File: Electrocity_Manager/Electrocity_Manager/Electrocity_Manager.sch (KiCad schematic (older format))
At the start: 187 parts, among them IC2 MAIN_SHUTDOWN, IC3 RELAY_STATE, IC4 ADC_RST, J1 SERIAL, P1 SWD, P10 EMERGENCY, P11 EMERGENCY, P12 FRAME_GRAND, P13 BATT_IN, P14 POWER_OUT, P15 FUN_OUT, P16 BATT_IN, P17 POWER_OUT, P18 FUN_OUT, P2 CAN, P3 CAN, P4 EMERGENCY_SIGNAL, P5 EMERGENCY_SIGNAL, P6 12V_OUT, P7 12V_OUT, P9 MAIN_SW, Q1 FET_N, Q2 NPN, Q3 NPN, Q7 FET_N, SW1 RST, SW2 SW0, SW3 SW1, U1 MAX3051, U10 BD9G101G, U11 ACS781, U12 V23134J1052D642, U13 ACS70331, U14 ACS781, U15 BD33FA1, U16 LOGO, U17 LOGO, U18 LOGO, U19 MCP2221A, U2 STM32F405RG, U20 OSRB38C9AA, U21 OSRB38C9AA, U22 HSIN_946, U23 LOGO, U3 FULL COLOR, U4 AQM0802_BL, U5 AP3211, U6 SI8900, U7 AZ1086H, U8 V23134J1052D642, U9 RPA60-12FW/P, X1 8MHz

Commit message: 緑ピカチュウか何か
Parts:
- added U24: LOGO, Mizz_lib:Pikatyuu_15x15, symbol Electrocity_Manager-rescue:LOGO-myDevice
- added U25: LOGO, Mizz_lib:MonsterBall_10x10_silk, symbol Electrocity_Manager-rescue:LOGO-myDevice
- added U26: LOGO, Mizz_lib:PiOtyu_silk_21.3x6.8, symbol Electrocity_Manager-rescue:LOGO-myDevice
- C32: value 470u -> 220u
- C35: value 470u -> 100u
- U9: value RPA60-12FW/P -> RPA60-12FW/N
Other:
- moved on the sheet: U16, U17, U18, U23
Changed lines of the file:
@@
 P 12675 8025
 F 0 "U9" H 12675 8590 50  0000 C CNN
-F 1 "RPA60-12FW/P" H 12675 8499 50  0000 C CNN
+F 1 "RPA60-12FW/N" H 12675 8499 50  0000 C CNN
 F 2 "Mizz_lib:RPA60-24xxSFW" H 12675 8025 50  0001 C CNN
 F 3 "" H 12675 8025 50  0001 C CNN
@@
 P 11825 7975
 F 0 "C32" H 11850 8075 50  0000 L CNN
-F 1 "470u" H 11850 7875 50  0000 L CNN
+F 1 "220u" H 11850 7875 50  0000 L CNN
 F 2 "Capacitors_ThroughHole:C_Radial_D6.3_L11.2_P2.5" H 11825 7975 60  0001 C CNN
 F 3 "" H 11825 7975 60  0000 C CNN
@@
 P 13525 7925
 F 0 "C35" H 13425 7825 50  0000 L CNN
-F 1 "470u" H 13325 8100 50  0000 L CNN
+F 1 "100u" H 13325 8100 50  0000 L CNN
 F 2 "Capacitors_ThroughHole:C_Radial_D6.3_L11.2_P2.5" H 13525 7925 60  0001 C CNN
 F 3 "" H 13525 7925 60  0000 C CNN
@@
 L Electrocity_Manager-rescue:LOGO-myDevice U17
 U 1 1 5D1B0D5D
-P 15475 800
-F 0 "U17" H 15753 853 60  0000 L CNN
-F 1 "LOGO" H 15753 747 60  0000 L CNN
-F 2 "Mizz_lib:Power_logo_Silk_5x5" H 15475 800 60  0001 C CNN
-F 3 "" H 15475 800 60  0000 C CNN
-	1    15475 800
+P 15525 800
+F 0 "U17" H 15803 853 60  0000 L CNN
+F 1 "LOGO" H 15803 747 60  0000 L CNN
+F 2 "Mizz_lib:Power_logo_Silk_5x5" H 15525 800 60  0001 C CNN
+F 3 "" H 15525 800 60  0000 C CNN
+	1    15525 800
 	1    0    0    -1
 $EndComp
@@
 L Electrocity_Manager-rescue:LOGO-myDevice U18
 U 1 1 5D1B1113
-P 15475 1375
-F 0 "U18" H 15753 1428 60  0000 L CNN
-F 1 "LOGO" H 15753 1322 60  0000 L CNN
-F 2 "Mizz_lib:Mini_Monster" H 15475 1375 60  0001 C CNN
-F 3 "" H 15475 1375 60  0000 C CNN
-	1    15475 1375
+P 15525 1375
+F 0 "U18" H 15803 1428 60  0000 L CNN
+F 1 "LOGO" H 15803 1322 60  0000 L CNN
+F 2 "Mizz_lib:Mini_Monster" H 15525 1375 60  0001 C CNN
+F 3 "" H 15525 1375 60  0000 C CNN
+	1    15525 1375
 	1    0    0    -1
 $EndComp
@@
 L Electrocity_Manager-rescue:LOGO-myDevice U16
 U 1 1 5CD3E880
-P 15475 1950
-F 0 "U16" H 15753 2003 60  0000 L CNN
-F 1 "LOGO" H 15753 1897 60  0000 L CNN
-F 2 "Mizz_lib:Robocon2019_30.0x30.0_silk" H 15475 1950 60  0001 C CNN
-F 3 "" H 15475 1950 60  0000 C CNN
-	1    15475 1950
+P 15525 1950
+F 0 "U16" H 15803 2003 60  0000 L CNN
+F 1 "LOGO" H 15803 1897 60  0000 L CNN
+F 2 "Mizz_lib:Robocon2019_30.0x30.0_silk" H 15525 1950 60  0001 C CNN
+F 3 "" H 15525 1950 60  0000 C CNN
+	1    15525 1950
 	1    0    0    -1
 $EndComp
@@
 L Electrocity_Manager-rescue:LOGO-myDevice U23
 U 1 1 5CD3FB17
-P 15475 2525
-F 0 "U23" H 15753 2578 60  0000 L CNN
-F 1 "LOGO" H 15753 2472 60  0000 L CNN
-F 2 "Mizz_lib:Battery_Killer_logo" H 15475 2525 60  0001 C CNN
-F 3 "" H 15475 2525 60  0000 C CNN
-	1    15475 2525
+P 15525 2525
+F 0 "U23" H 15803 2578 60  0000 L CNN
+F 1 "LOGO" H 15803 2472 60  0000 L CNN
+F 2 "Mizz_lib:Battery_Killer_logo" H 15525 2525 60  0001 C CNN
+F 3 "" H 15525 2525 60  0000 C CNN
+	1    15525 2525
 	1    0    0    -1
 $EndComp
@@
 	11800 6650 12000 6650
 Connection ~ 12000 6650
+$Comp
+L Electrocity_Manager-rescue:LOGO-myDevice U24
+U 1 1 5CC98F30
+P 15525 3100
+F 0 "U24" H 15803 3153 60  0000 L CNN
+F 1 "LOGO" H 15803 3047 60  0000 L CNN
+F 2 "Mizz_lib:Pikatyuu_15x15" H 15525 3100 60  0001 C CNN
+F 3 "" H 15525 3100 60  0000 C CNN
+	1    15525 3100
+	1    0    0    -1
+$EndComp
+$Comp
+L Electrocity_Manager-rescue:LOGO-myDevice U25
+U 1 1 5CC9B168
+P 15525 3700
+F 0 "U25" H 15803 3753 60  0000 L CNN
+F 1 "LOGO" H 15803 3647 60  0000 L CNN
+F 2 "Mizz_lib:MonsterBall_10x10_silk" H 15525 3700 60  0001 C CNN
+F 3 "" H 15525 3700 60  0000 C CNN
+	1    15525 3700
+	1    0    0    -1
+$EndComp
+$Comp
+L Electrocity_Manager-rescue:LOGO-myDevice U26
+U 1 1 5CC9CF8E
+P 15525 4300
+F 0 "U26" H 15803 4353 60  0000 L CNN
+F 1 "LOGO" H 15803 4247 60  0000 L CNN
+F 2 "Mizz_lib:PiOtyu_silk_21.3x6.8" H 15525 4300 60  0001 C CNN
+F 3 "" H 15525 4300 60  0000 C CNN
+	1    15525 4300
+	1    0    0    -1
+$EndComp
 $EndSCHEMATC

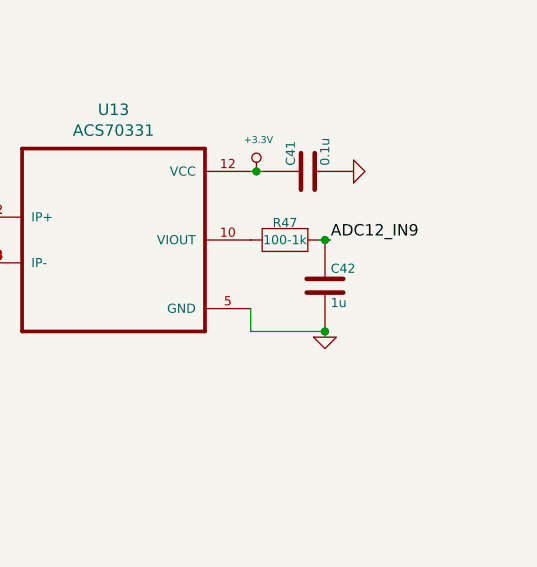
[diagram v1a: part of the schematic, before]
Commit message: ピカチュウたちの配線を変えた。
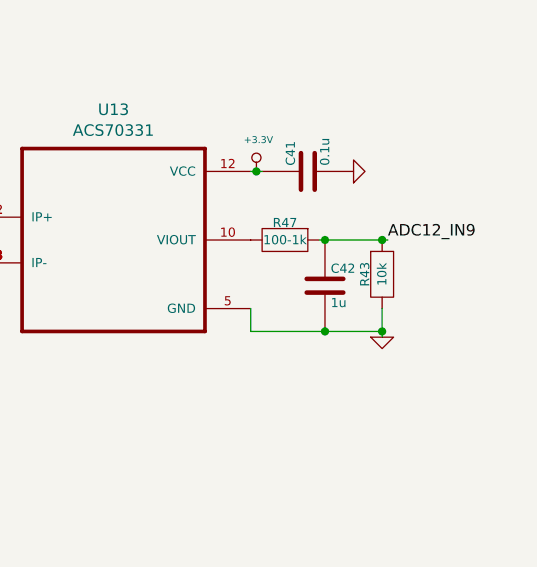
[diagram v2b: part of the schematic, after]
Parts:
- added R43: 10k, Mizz_lib:R_0603, symbol device:R
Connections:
- net ADC12_IN9: now also R43.1
- net GND: now also R43.2
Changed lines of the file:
@@
 L power:GND #PWR0105
 U 1 1 5CF8E453
-P 15250 8650
-F 0 "#PWR0105" H 15250 8650 30  0001 C CNN
-F 1 "GND" H 15250 8580 30  0001 C CNN
-F 2 "" H 15250 8650 60  0000 C CNN
-F 3 "" H 15250 8650 60  0000 C CNN
-	1    15250 8650
+P 15500 8650
+F 0 "#PWR0105" H 15500 8650 30  0001 C CNN
+F 1 "GND" H 15500 8580 30  0001 C CNN
+F 2 "" H 15500 8650 60  0000 C CNN
+F 3 "" H 15500 8650 60  0000 C CNN
+	1    15500 8650
 	1    0    0    -1
 $EndComp
@@
 $EndComp
 Wire Wire Line
-	15250 8650 15250 8625
-Wire Wire Line
 	14925 8525 14925 8625
 Wire Wire Line
 	14925 8625 15250 8625
-Connection ~ 15250 8625
-Wire Wire Line
-	15275 8225 15250 8225
 Connection ~ 15250 8225
 Wire Wire Line
@@
 Text Label 14650 4075 2    50   ~ 0
 ADC12_IN2
-Text Label 15275 8225 0    50   ~ 0
+Text Label 15525 8225 0    50   ~ 0
 ADC12_IN9
 Text Label 4500 8750 2    50   ~ 0
@@
 	1    0    0    -1
 $EndComp
+$Comp
+L device:R R43
+U 1 1 5CCDE331
+P 15500 8375
+F 0 "R43" V 15425 8375 40  0000 C CNN
+F 1 "10k" V 15500 8375 40  0000 C CNN
+F 2 "Mizz_lib:R_0603" V 15430 8375 30  0001 C CNN
+F 3 "" H 15500 8375 30  0000 C CNN
+	1    15500 8375
+	1    0    0    -1
+$EndComp
+Wire Wire Line
+	15250 8625 15500 8625
+Wire Wire Line
+	15500 8625 15500 8650
+Connection ~ 15250 8625
+Wire Wire Line
+	15500 8625 15500 8525
+Connection ~ 15500 8625
+Wire Wire Line
+	15500 8225 15525 8225
+Wire Wire Line
+	15250 8225 15500 8225
+Connection ~ 15500 8225
 $EndSCHEMATC
